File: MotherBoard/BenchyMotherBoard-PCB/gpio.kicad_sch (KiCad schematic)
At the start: 4 parts

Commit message: Add MORE regulators, USB, Display, and SDCard
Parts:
- added C?: 4.7uF, Capacitor_SMD:C_0805_2012Metric, symbol Device:C_Small
- added J?: Micro_SD_Card_Det, Daxxn_Connectors:microSD_HC_Molex_47219-2001, symbol Connector:Micro_SD_Card_Det
- added J?: BOOT2-CONN, Connector_PinHeader_2.54mm:PinHeader_1x03_P2.54mm_Vertical, symbol Connector:Conn_01x03_Male
- added J?: BOOT1-CONN, Connector_PinHeader_2.54mm:PinHeader_1x03_P2.54mm_Vertical, symbol Connector:Conn_01x03_Male
- added J?: Conn_SWD_10, Connector:Tag-Connect_TC2050-IDC-FP_2x05_P1.27mm_Vertical, symbol Connector:Conn_ARM_JTAG_SWD_10
- added J?: BOOT0-CONN, Connector_PinHeader_2.54mm:PinHeader_1x03_P2.54mm_Vertical, symbol Connector:Conn_01x03_Male
- added R? (x3): 100, Resistor_SMD:R_0402_1005Metric, symbol Device:R_Small_US
- added R? (x5): 47K, Resistor_SMD:R_0402_1005Metric, symbol Device:R_Small_US
- added R? (x2): 10K, Resistor_SMD:R_0402_1005Metric, symbol Device:R_Small_US
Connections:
- net SDMMC-D2: now reaches U?.B3 (PE6)
- net SDMMC-D2: now also J?.1 (DAT2), R?.2
- net SWO: now reaches U?.D14 (SWO-TRACE)
- net SWO: now also J?.6 (SWO/TDO)
- net SWDIO: now reaches U?.D15 (SWDIO)
- net SWDIO: now also J?.2 (SWDIO/TMS)
- net SWDCLK: now reaches U?.D16 (SWCLK)
- net SWDCLK: now also J?.4 (SWDCLK/TCK)
- net at U?.J1 (~{RST}): now also R?.2
- net at U?.K1 (BOOT0): now also R?.2
- net at U?.K4 (BOOT1): now also R?.2
- net at U?.L2 (BOOT2): now also R?.2
- net GND: now reaches U?.T15 (BYPASS-REG1V8)
- net GND: now also C?.2, J?.11 (SHIELD), J?.3 (GND), J?.3 (Pin_3), J?.3 (Pin_3), J?.3 (Pin_3), J?.5 (GND), J?.6 (VSS), J?.9 (DET_B), J?.9 (GNDDetect)
- net SDMMC-D1: now reaches U?.A10 (PC9)
- net SDMMC-D1: now also J?.8 (DAT1), R?.2
- net SDMMC-D3: now reaches U?.A11 (PC11)
- net SDMMC-D3: now also J?.2 (DAT3/CD), R?.2
- net SDMMC-CMD: now reaches U?.B10 (PD2)
- net SDMMC-CMD: now also J?.3 (CMD), R?.2
- net SDMMC-CLK: now reaches U?.C10 (PC12)
- net SDMMC-CLK: now also J?.5 (CLK), R?.2
- net SDMMC-D0: now reaches U?.C11 (PC8)
- net SDMMC-D0: now also J?.7 (DAT0), R?.2
- net SD-CARD-DETECT: now reaches U?.D11 (PC10)
- net SD-CARD-DETECT: now also J?.10 (DET_A)
- new net: J?.2 (Pin_2), R?.1 (x3)
- new net RESET: J?.10 (~{RESET})
- new net VDD: C?.1, J?.1 (Pin_1), J?.1 (Pin_1), J?.1 (Pin_1), J?.1 (VTref), J?.4 (VDD), R?.1, R?.1, R?.1, R?.1, R?.1, R?.1, R?.1
- no-connect marks 0 -> 2
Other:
- note added: "DEFAULT: SDCARD SDMMC1 BOOT0: 1 BOOT1: 0 BOOT2: 1"
- moved on the sheet: U?E

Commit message: Initial schematic lock
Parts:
- removed J?: Conn_SWD_10, Connector:Tag-Connect_TC2050-IDC-FP_2x05_P1.27mm_Vertical, symbol Connector:Conn_ARM_JTAG_SWD_10
- removed R?: 10K, Resistor_SMD:R_0402_1005Metric, symbol Device:R_Small_US
- added C133, C134, C137, C138: 15pF, Capacitor_SMD:C_0402_1005Metric, symbol Device:C_Small
- added C135: 1nF, Capacitor_SMD:C_0402_1005Metric, symbol Device:C_Small
- added C136: 10nF, Capacitor_SMD:C_0402_1005Metric, symbol Device:C_Small
- added C?: 4.7uF, Capacitor_SMD:C_0805_2012Metric, symbol Device:C_Small
- added J2: SWD-TAG, Connector:Tag-Connect_TC2050-IDC-FP_2x05_P1.27mm_Vertical, symbol Daxxn_Connectors:SWD-TAG
- added J?: Micro_SD_Card_Det, Daxxn_Connectors:microSD_HC_Molex_47219-2001, symbol Connector:Micro_SD_Card_Det
- added R? (x5): 47K, Resistor_SMD:R_0402_1005Metric, symbol Device:R_Small_US
- added R?: 10K, Resistor_SMD:R_0402_1005Metric, symbol Device:R_Small_US
- added Y1: 24MHz, Daxxn_Passives:Crystal_SMD_4Pin_3.2x2.5mm, symbol Device:Crystal_GND24_Small
- added Y2: 32.7KHz, Daxxn_Passives:Crystal_SMD_4Pin_3.2x2.5mm, symbol Device:Crystal_GND24_Small
- gave numbers to parts that had none: 15
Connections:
- net GND: now also C133.1, C134.2, C136.1, C137.1, C138.2, C?.2, J2.3 (GND), J2.5 (GND), J2.9 (GNDDetect), J?.11 (SHIELD), J?.6 (VSS), J?.9 (DET_B), Y1.2, Y1.4, Y2.2, Y2.4; no longer U2.T15 (BYPASS-REG1V8)
- net RESET: now also U2.J1 (~{RST}), C135.2, C136.2, J2.10 (~{RESET})
- net SDMMC-CMD: no longer J3.3 (CMD), R79.2
- net SWDCLK: now also J2.4 (SWDCLK)
- net SWDIO: now also J2.2 (SWDIO)
- net SWO: now also J2.6 (SWO)
- net VDD: now also C?.1, J2.1 (Vref), J?.4 (VDD), R?.1, R?.1, R?.1, R?.1, R?.1, R?.1
- net SD-BOOT-D2: now reaches U2.A7 (PB3)
- net SD-BOOT-D2: now also J?.1 (DAT2), R?.2
- net SD-BOOT-D1: now reaches U2.A8 (PB15)
- net SD-BOOT-D1: now also J?.8 (DAT1), R?.2
- net DISP-USB-BUS.USB-SDA: now reaches U2.B5 (PB7)
- net COMMS.LOGIC-SCK: now reaches U2.B8 (PA8)
- net SD-BOOT-D3: now reaches U2.B9 (PB4)
- net SD-BOOT-D3: now also J?.2 (DAT3/CD), R?.2
- net SD-BOOT-DETECT: now reaches U2.C9 (PB14)
- net SD-BOOT-DETECT: now also J?.10 (DET_A)
- net DISP-USB-BUS.USB-SCK: now reaches U2.T12 (PB6)
- net COMMS.MAINS-4: now reaches U2.T6 (PA7)
- net COMMS.MAINS-1: now reaches U2.T8 (PB5)
- net COMMS.MAINS-2: now reaches U2.T9 (PB13)
- net COMMS.RELAY-SDA: now reaches U2.U16 (PA12)
- net COMMS.PWR-SDA: now reaches U2.V1 (PB11)
- net COMMS.RELAY-SCK: now reaches U2.V17 (PA11)
- net PWR-BUS.TX: now reaches U2.W2 (PA2)
- net COMMS.PWR-SCK: now reaches U2.W5 (PB10)
- net SD-FILES-CLK: now reaches U2.A2 (PG15)
- net SD-FILES-CLK: now also J3.5 (CLK), R76.2
- net SD-BOOT-CLK: now reaches U2.A5 (PE3)
- net SD-BOOT-CLK: now also J?.5 (CLK), R?.2
- net SD-BOOT-CMD: now reaches U2.A6 (PG6)
- net SD-BOOT-CMD: now also J?.3 (CMD), R?.2
- net COMMS.ELOAD-SCK: now reaches U2.T1 (PE2)
- net COMMS.MAINS-5: now reaches U2.T10 (PE7)
- net COMMS.MAINS-6: now reaches U2.T11 (PE8)
- net at U2.J2 (~{RST-CORE}): now also C135.1
- net at U2.M1 (OSC-IN): now also C133.2, Y1.1
- net at U2.M2 (OSC-OUT): now also C134.1, Y1.3
- net SD-FILES-CMD: now reaches U2.A3 (PD0)
- net SD-FILES-CMD: now also J3.3 (CMD), R79.2
- net SD-FILES-D0: now reaches U2.A4 (PD1)
- net SD-FILES-D0: now also J3.7 (DAT0), R77.2
- net SD-FILES-D3: now reaches U2.B4 (PD7)
- net SD-FILES-D3: now also J3.2 (DAT3/CD), R80.2
- net SD-FILES-DETECT: now reaches U2.C6 (PD3)
- net SD-FILES-DETECT: now also J3.10 (DET_A)
- net SD-FILES-D1: now reaches U2.D6 (PD4)
- net SD-FILES-D1: now also J3.8 (DAT1), R78.2
- net SD-FILES-D2: now reaches U2.D7 (PD5)
- net SD-FILES-D2: now also J3.1 (DAT2), R81.2
- net PWR-BUS.RX: now reaches U2.E3 (PD6)
- net at U2.H1 (PC14): now also C137.2, Y2.1
- net at U2.H2 (PC15): now also C138.1, Y2.3
- net COMMS.MAINS-3: now reaches U2.T7 (PC0)
- net COMMS.ELOAD-SDA: now reaches U2.U12 (PD13)
- net SD-CARD-DETECT: no longer names the net of U2.D11 (PC10)
- net SD-CARD-DETECT: no longer J3.10 (DET_A)
- removed net SDMMC-CLK: J3.5 (CLK), R76.2, U2.C10 (PC12)
- removed net SDMMC-D0: J3.7 (DAT0), R77.2, U2.C11 (PC8)
- removed net SDMMC-D1: J3.8 (DAT1), R78.2, U2.A10 (PC9)
- removed net SDMMC-D2: J3.1 (DAT2), R81.2, U2.B3 (PE6)
- removed net SDMMC-D3: J3.2 (DAT3/CD), R80.2, U2.A11 (PC11)
- new net COMMS.LOGIC-SDA: U2.A10 (PC9)
- new net SD-BOOT-D0: J?.7 (DAT0), R?.2, U2.B3 (PE6)
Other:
- moved on the sheet: C132, J3, J4, J5, J6, R76, R77, R78, R79, R80, R81, R82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

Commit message: (WIP) Start layout
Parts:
- removed J3, J?: Micro_SD_Card_Det, Daxxn_Connectors:microSD_HC_Molex_47219-2001, symbol Connector:Micro_SD_Card_Det
- added J3: FILES-SD-CARD, Daxxn_Connectors:microSD_HC_Molex_47219-2001, symbol Connector:Micro_SD_Card
- added J7: BOOT-SD-CARD, Daxxn_Connectors:microSD_HC_Molex_47219-2001, symbol Connector:Micro_SD_Card
- added J8: FAN-CONN, Connector_JST:JST_NV_B02P-NV_1x02_P5.00mm_Vertical, symbol Connector:Conn_01x02_Male
- added Q1: SQ2310ES_SOT23, Package_TO_SOT_SMD:SOT-23, symbol Daxxn_Transistors:SQ2310ES_SOT23
- added Q2: MMBT2222A, Package_TO_SOT_SMD:SOT-23, symbol Daxxn_Transistors:MMBT2222A
- added R91: 10K, Resistor_SMD:R_0402_1005Metric, symbol Device:R_Small_US
- added R92: 100, Resistor_SMD:R_0402_1005Metric, symbol Device:R_Small_US
- added R93: 1K, Resistor_SMD:R_0402_1005Metric, symbol Device:R_Small_US
- gave numbers to parts that had none: 7
- renumbered C132 to C133, C133 to C134, C134 to C135, C135 to C136, C136 to C137, C137 to C139, C138 to C140
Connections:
- net GND: now also J3.6 (VSS), J3.9 (SHIELD), J7.6 (VSS), J7.9 (SHIELD), Q1.2 (S), Q2.1 (E)
- net SD-BOOT-CLK: now also J7.5 (CLK)
- net SD-BOOT-CMD: now also J7.3 (CMD)
- net SD-BOOT-D0: now also J7.7 (DAT0)
- net SD-BOOT-D1: now also J7.8 (DAT1)
- net SD-BOOT-D2: now also J7.1 (DAT2)
- net SD-BOOT-D3: now also J7.2 (DAT3/CD)
- net SD-FILES-CLK: now also J3.5 (CLK)
- net SD-FILES-CMD: now also J3.3 (CMD)
- net SD-FILES-D0: now also J3.7 (DAT0)
- net SD-FILES-D1: now also J3.8 (DAT1)
- net SD-FILES-D2: now also J3.1 (DAT2)
- net SD-FILES-D3: now also J3.2 (DAT3/CD)
- net VDD: now also J3.4 (VDD), J7.4 (VDD)
- net FAN-PWM: now reaches U2.C1 (PE11)
- net FAN-PWM: now also R93.2
- new net: Q2.2 (B), R93.1
- new net: Q2.3 (C), R91.1, R92.1
- new net: J8.2 (Pin_2), Q1.3 (D)
- new net: Q1.1 (G), R92.2
- new net VCC: R91.2
- new net VPWR: J8.1 (Pin_1)
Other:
- title: Benchy Version 2 -> Benchy Reloaded

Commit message: (WIP) Replaced DDR VRef with reg and started layout
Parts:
- J8: footprint Connector_JST:JST_NV_B02P-NV_1x02_P5.00mm_Vertical -> Connector_PinHeader_2.54mm:PinHeader_1x02_P2.54mm_Vertical
- renumbered C133 to C137, C134 to C138, C135 to C139, C136 to C140, C137 to C141, C138 to C142, C139 to C143, C140 to C144, R76 to R73, R77 to R74, R78 to R75, R79 to R76, R80 to R77, R81 to R78, R82 to R79, R83 to R80, R84 to R81, R85 to R82, R86 to R83, R87 to R84, R88 to R85, R89 to R86, R90 to R87, R91 to R88, R92 to R89, R93 to R90, U2 to U1
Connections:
- net PWR-BUS.RX: no longer U1.E3 (PD6)
- net PWR-BUS.TX: no longer U1.W2 (PA2)
- net BOOT0-JMP: now reaches J4.2 (Pin_2), R79.1
- net USB-BUS.RESET: now reaches U1.T13 (PB2)
- net BOOT2-JMP: now reaches J6.2 (Pin_2), R81.1
- net DISP-BUS.RESET: now reaches U1.B11 (PE4)
- net DISP-BUS.BRIGHT: now reaches U1.C2 (PE13)
- net BOOT1-JMP: now reaches J5.2 (Pin_2), R80.1
- net DISP-BUS.TE: now reaches U1.D10 (PC6)
- net COMMS.ELOAD-SCK renamed ELOAD-BUS.SCK
- net COMMS.ELOAD-SDA renamed ELOAD-BUS.SDA
- net COMMS.LOGIC-SCK renamed LOGIC-BUS.SCK
- net COMMS.LOGIC-SDA renamed LOGIC-BUS.SDA
- net COMMS.MAINS-1 renamed RELAY-BUS.1
- net COMMS.MAINS-2 renamed RELAY-BUS.2
- net COMMS.MAINS-3 renamed RELAY-BUS.3
- net COMMS.MAINS-4 renamed RELAY-BUS.4
- net COMMS.MAINS-5 renamed RELAY-BUS.5
- net COMMS.MAINS-6 renamed RELAY-BUS.6
- net COMMS.PWR-SCK renamed PWR-BUS.SCK
- net COMMS.PWR-SDA renamed PWR-BUS.SDA
- net COMMS.RELAY-SCK renamed SWITCHER-BUS.SCK
- net COMMS.RELAY-SDA renamed SWITCHER-BUS.SDA
- net DISP-USB-BUS.USB-SCK renamed USB-BUS.SCK
- net DISP-USB-BUS.USB-SDA renamed USB-BUS.SDA
- new net SM-BUS.RX: U1.E3 (PD6)
- new net SM-BUS.TX: U1.W2 (PA2)
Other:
- moved on the sheet: J4, J5, J6, R80, R81

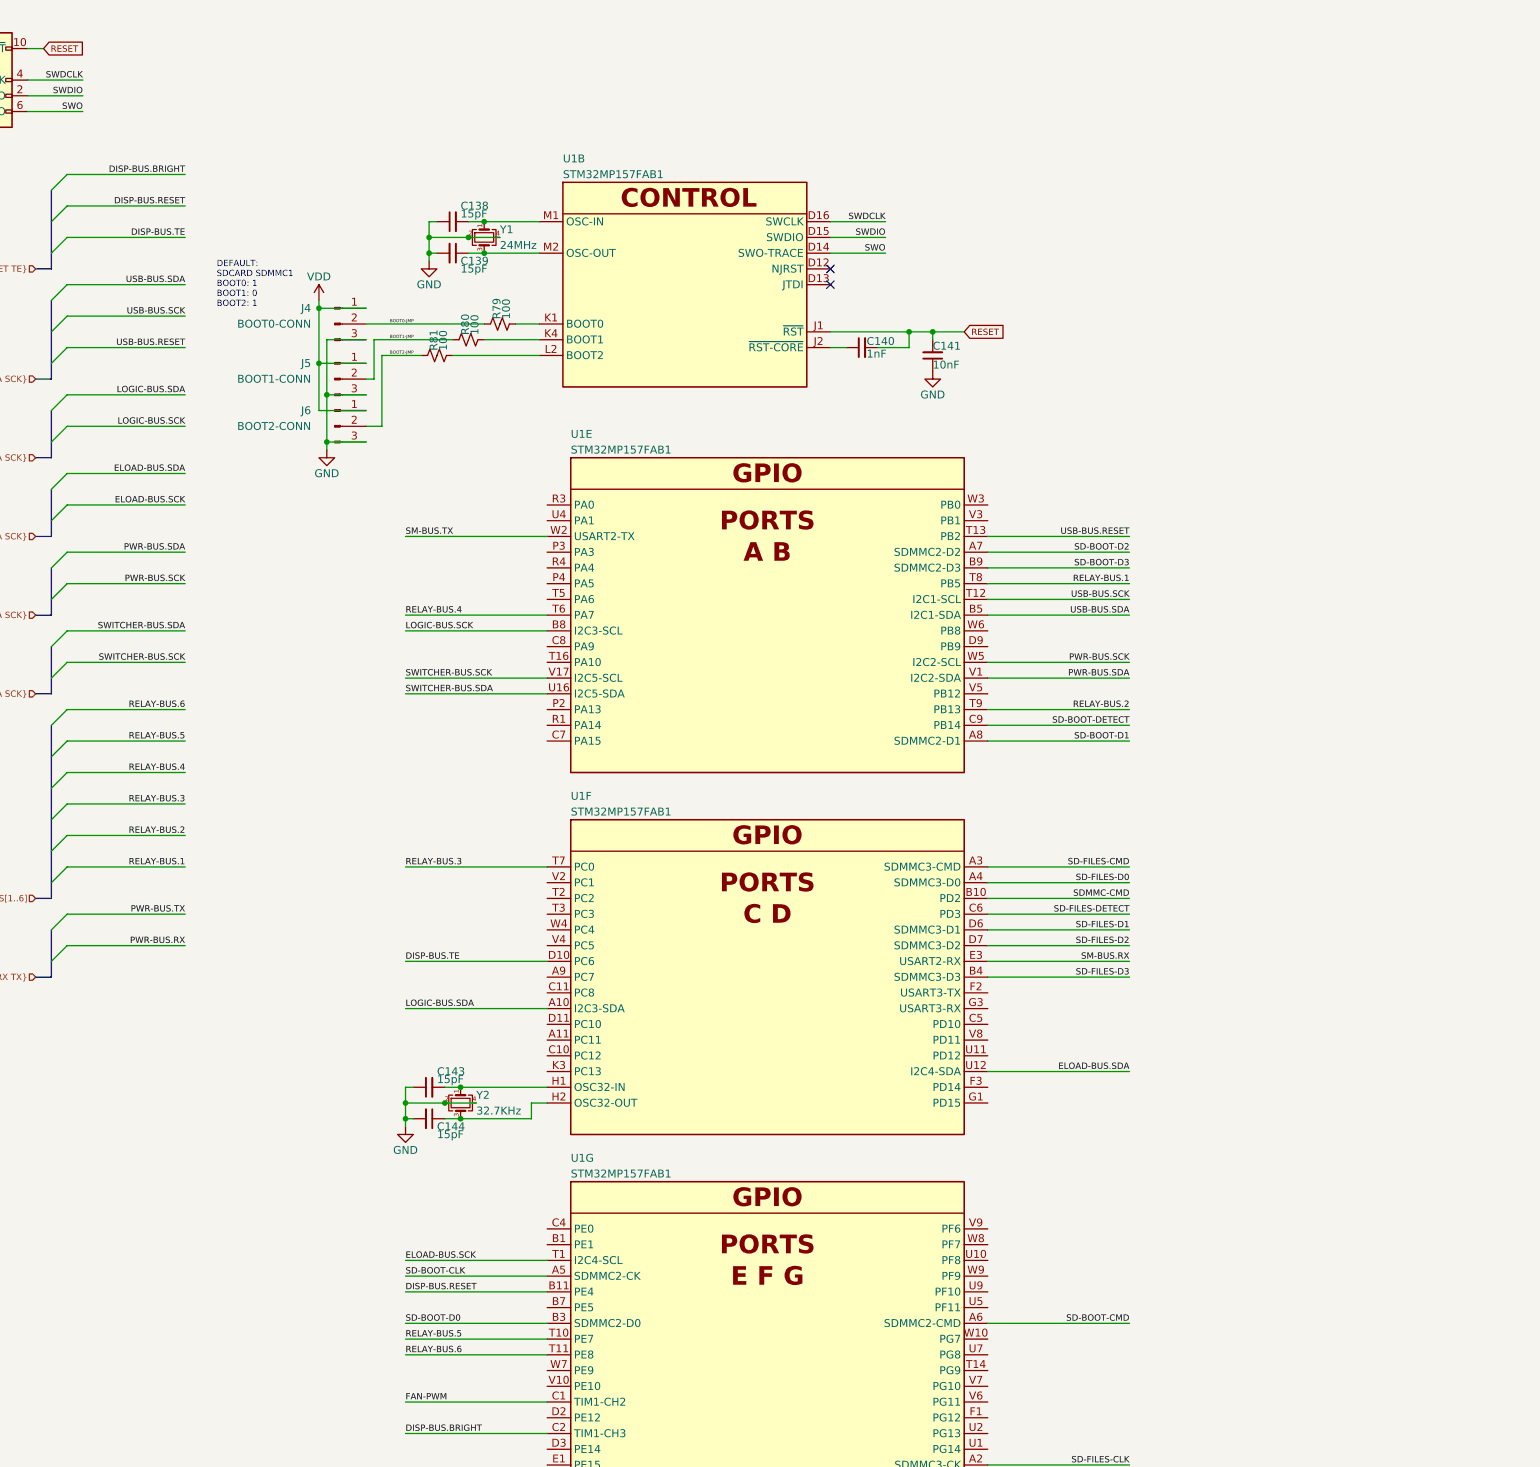
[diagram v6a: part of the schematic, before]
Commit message: Mostly routed USB
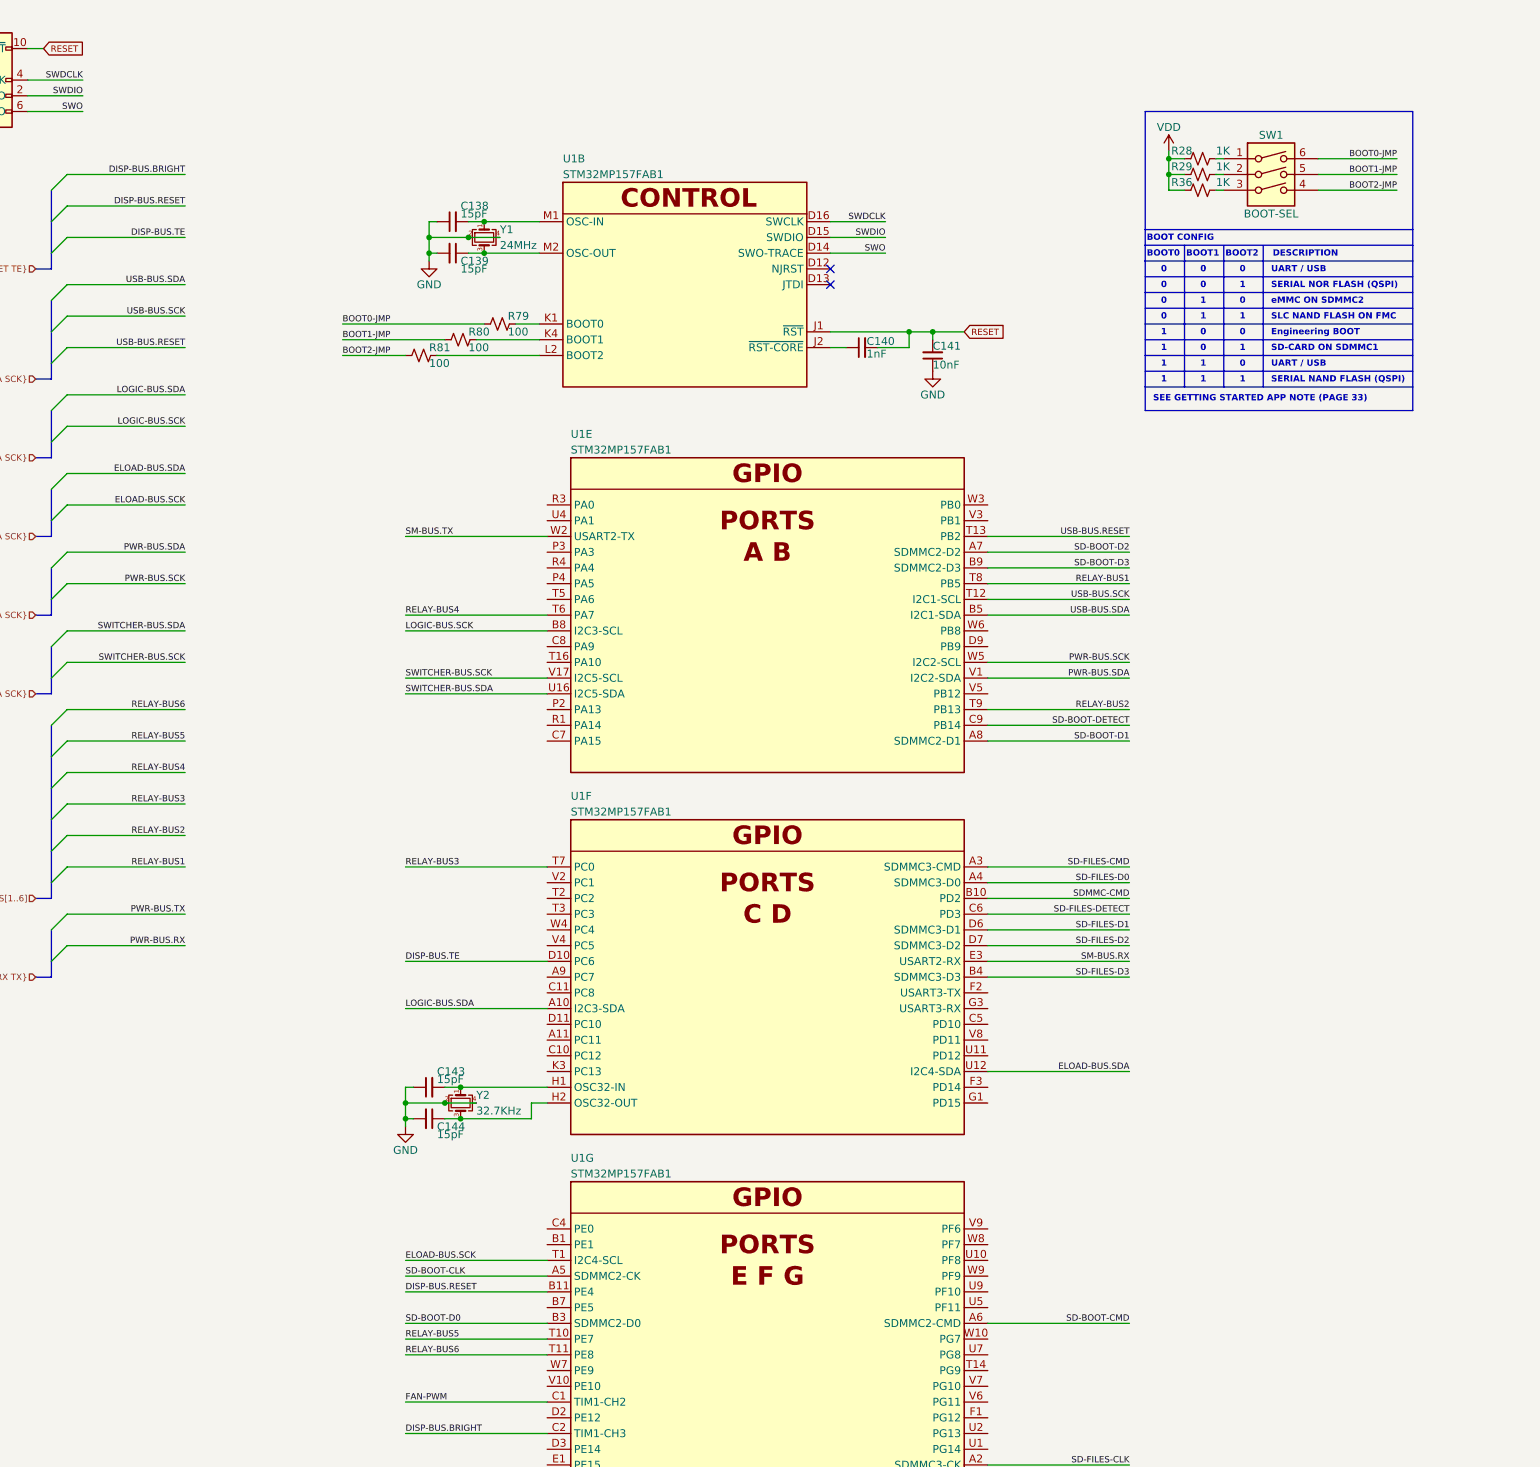
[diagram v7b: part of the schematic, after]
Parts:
- removed J4: BOOT0-CONN, Connector_PinHeader_2.54mm:PinHeader_1x03_P2.54mm_Vertical, symbol Connector:Conn_01x03_Male
- removed J5: BOOT1-CONN, Connector_PinHeader_2.54mm:PinHeader_1x03_P2.54mm_Vertical, symbol Connector:Conn_01x03_Male
- removed J6: BOOT2-CONN, Connector_PinHeader_2.54mm:PinHeader_1x03_P2.54mm_Vertical, symbol Connector:Conn_01x03_Male
- added R28, R29, R36: 1K, Resistor_SMD:R_0402_1005Metric, symbol Device:R_Small_US
- added SW1: BOOT-SEL, Button_Switch_SMD:SW_DIP_SPSTx03_Slide_Copal_CVS-03xB_W5.9mm_P1mm, symbol Switch:SW_DIP_x03
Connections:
- net BOOT0-JMP: now also SW1.6
- net BOOT1-JMP: now also SW1.5
- net BOOT2-JMP: now also SW1.4
- net VDD: now also R28.1, R29.1, R36.1
- net RELAY-BUS.1 renamed RELAY-BUS1
- net RELAY-BUS.2 renamed RELAY-BUS2
- net RELAY-BUS.3 renamed RELAY-BUS3
- net RELAY-BUS.4 renamed RELAY-BUS4
- net RELAY-BUS.5 renamed RELAY-BUS5
- net RELAY-BUS.6 renamed RELAY-BUS6
- new net: R28.2, SW1.1
- new net: R29.2, SW1.2
- new net: R36.2, SW1.3
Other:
- note added: "0"
- note added: "1"
- note added: "BOOT CONFIG"
- note added: "BOOT0"
- note added: "BOOT1"
- note added: "BOOT2"
- note added: "DESCRIPTION"
- note added: "Engineering BOOT"
- note added: "SD-CARD ON SDMMC1"
- note added: "SEE GETTING STARTED APP NOTE (PAGE 33)"
- note added: "SERIAL NAND FLASH (QSPI)"
- note added: "SERIAL NOR FLASH (QSPI)"
- note added: "SLC NAND FLASH ON FMC"
- note added: "UART / USB"
- note added: "eMMC ON SDMMC2"
- note removed: "DEFAULT: SDCARD SDMMC1 BOOT0: 1 BOOT1: 0 BOOT2: 1"
- moved on the sheet: R80, R81

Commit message: Most routing completed
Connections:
- net SD-FILES-DETECT: no longer names the net of U1.C6 (PD3)
- net SDMMC-CMD: no longer names the net of U1.B10 (PD2)
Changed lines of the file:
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@@
-    (stroke (width 0) (type default))
-  )
-  (wire (pts (xy 195.58 167.64) (xy 218.44 167.64))
     (stroke (width 0) (type default))
   )
@@
   )
   (wire (pts (xy 195.58 111.76) (xy 218.44 111.76))
-    (stroke (width 0) (type default))
-  )
-  (wire (pts (xy 195.58 165.1) (xy 218.44 165.1))
     (stroke (width 0) (type default))
   )
@@
     (effects (font (size 1.016 1.016)) (justify right bottom))
   )
-  (label "SD-FILES-DETECT" (at 218.44 167.64 180) (fields_autoplaced)
-    (effects (font (size 1.016 1.016)) (justify right bottom))
-  )
   (label "SD-BOOT-D2" (at 218.44 109.22 180) (fields_autoplaced)
     (effects (font (size 1.016 1.016)) (justify right bottom))
@@
     (effects (font (size 1.016 1.016)) (justify left bottom))
   )
-  (label "SDMMC-CMD" (at 218.44 165.1 180) (fields_autoplaced)
-    (effects (font (size 1.016 1.016)) (justify right bottom))
-  )
   (label "SD-BOOT-CMD" (at 454.66 113.03 0) (fields_autoplaced)
